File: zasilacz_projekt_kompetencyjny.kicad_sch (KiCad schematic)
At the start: 0 parts

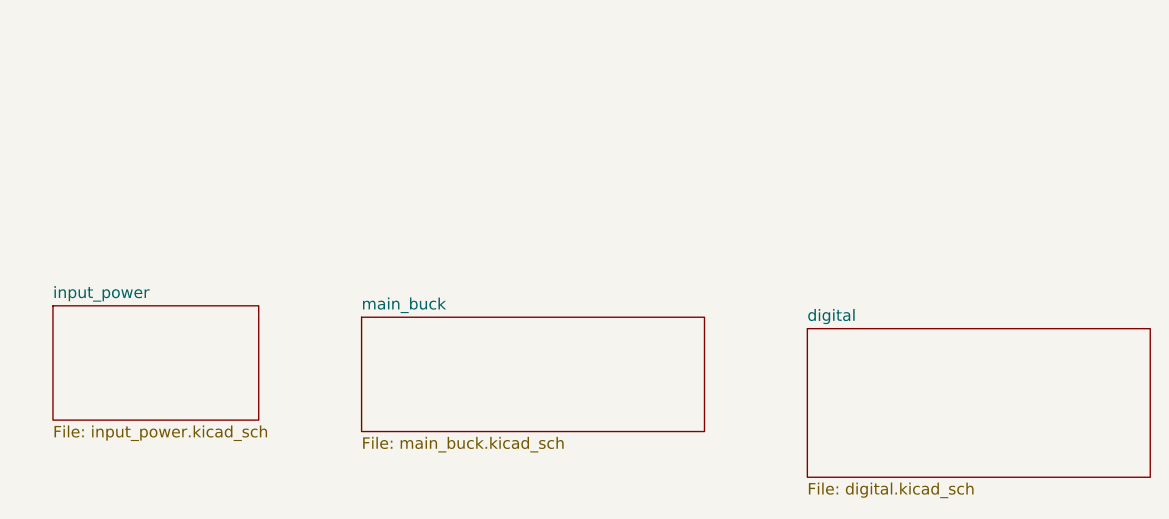
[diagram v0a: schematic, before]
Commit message: dodanie zasilania pomocniczego 10v oraz 5v i
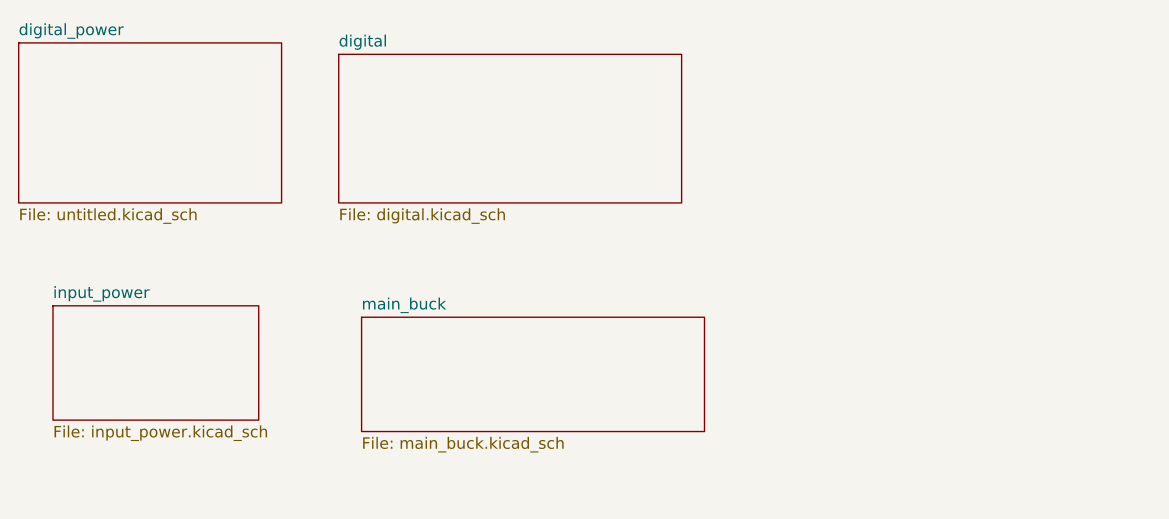
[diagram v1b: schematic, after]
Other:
- added sheet digital_power (untitled.kicad_sch)
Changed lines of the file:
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@@
+	)
+	(sheet
+		(at 64.77 48.26)
+		(size 29.21 17.78)
+		(exclude_from_sim no)
+		(in_bom yes)
+		(on_board yes)
+		(dnp no)
+		(fields_autoplaced yes)
+		(stroke
+			(width 0.1524)
+			(type solid)
+		)
+		(fill
+			(color 0 0 0 0.0000)
+		)
+		(property "Sheetname" "digital_power"
+			(at 64.77 47.5484 0)
+			(effects
+				(font
+					(size 1.27 1.27)
+				)
+				(justify left bottom)
+			)
+		)
+		(property "Sheetfile" "untitled.kicad_sch"
+			(at 64.77 66.6246 0)
+			(effects
+				(font
+					(size 1.27 1.27)
+				)
+				(justify left top)
+			)
+		)
+		(instances
+			(project "zasilacz_projekt_kompetencyjny"
+				(path "/e9ad3936-200e-4b7c-85fb-533ca6ea54fd"
+					(page "5")
+				)
+			)
+		)
 	)
 	(sheet
@@
 	)
 	(sheet
-		(at 152.4 80.01)
+		(at 100.33 49.53)
 		(size 38.1 16.51)
 		(exclude_from_sim no)
@@
 		)
 		(property "Sheetname" "digital"
-			(at 152.4 79.2984 0)
+			(at 100.33 48.8184 0)
 			(effects
 				(font
@@
 		)
 		(property "Sheetfile" "digital.kicad_sch"
-			(at 152.4 97.1046 0)
+			(at 100.33 66.6246 0)
 			(effects
 				(font
